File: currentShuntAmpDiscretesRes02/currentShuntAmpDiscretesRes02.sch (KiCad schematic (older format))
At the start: 17 parts, among them Q1 2N3906, Q2 2N3906, Q3 2N3906

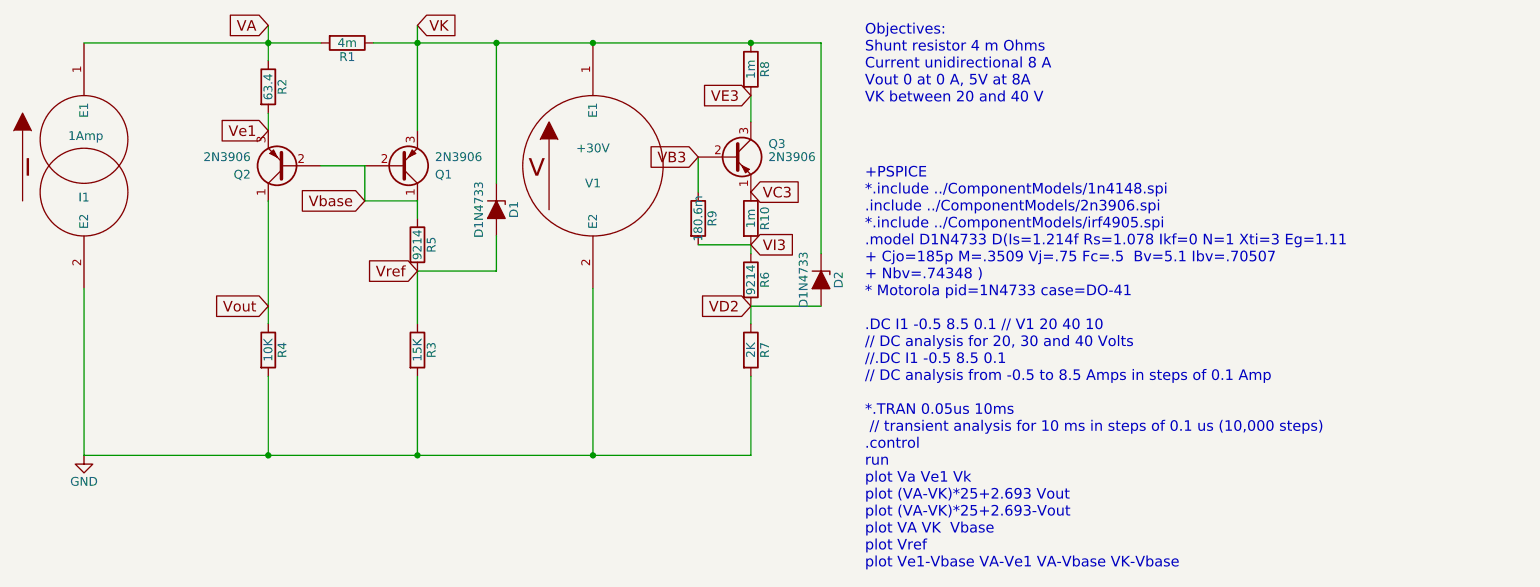
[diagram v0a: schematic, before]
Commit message: spice and spreadsheet models lined up approximately
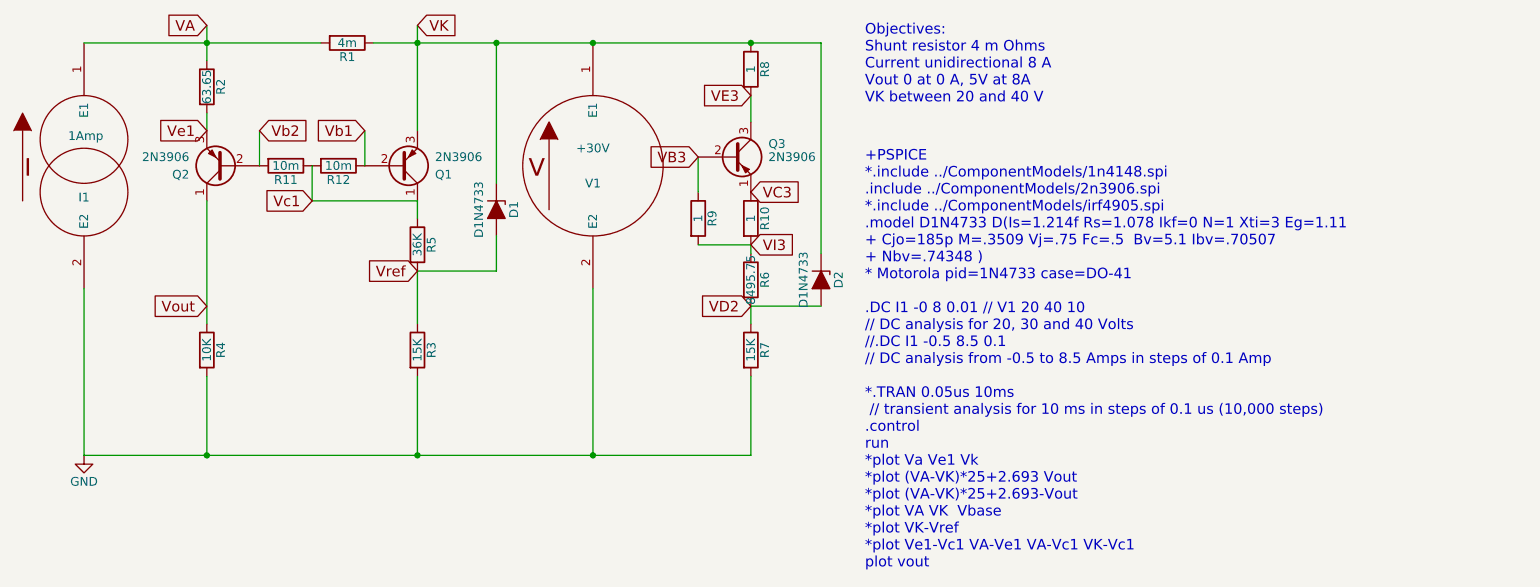
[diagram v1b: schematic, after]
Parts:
- added R11, R12: 10m, symbol R
- R10, R8: value 1m -> 1
- R2: value 63.4 -> 63.65
- R5: value 9214 -> 36K
- R6: value 9214 -> 8495.75
- R7: value 2K -> 15K
- R9: value 180.6m -> 1
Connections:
- net Vbase renamed Vc1
- net Vc1: now also R11.1, R12.2; no longer Q1.2 (B), Q2.2 (B)
- new net Vb1: Q1.2 (B), R12.1
- new net Vb2: Q2.2 (B), R11.2
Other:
- note added: "+PSPICE \n*.include ../ComponentModels/1n4148.spi\n.include ../ComponentModels/2n3906.spi\n*.include ../ComponentModels/irf4905.spi\n.model D1N4733 D(Is=1.214f Rs=1.078 Ikf=0 N=1 Xti=3 Eg=1.11\n+ Cjo=185p M=.3509 Vj=.75 Fc=.5 Bv=5.1 Ibv=.70507\n+ Nbv=.74348 )\n* Motorola pid=1N4733 case=DO-41\n\n.DC I1 -0 8 0.01 // V1 20 40 10 \n// DC analysis for 20, 30 and 40 Volts\n//.DC I1 -0.5 8.5 0.1\n// DC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"
- note removed: "+PSPICE \n*.include ../ComponentModels/1n4148.spi\n.include ../ComponentModels/2n3906.spi\n*.include ../ComponentModels/irf4905.spi\n.model D1N4733 D(Is=1.214f Rs=1.078 Ikf=0 N=1 Xti=3 Eg=1.11\n+ Cjo=185p M=.3509 Vj=.75 Fc=.5 Bv=5.1 Ibv=.70507\n+ Nbv=.74348 )\n* Motorola pid=1N4733 case=DO-41\n\n.DC I1 -0.5 8.5 0.1 // V1 20 40 10 \n// DC analysis for 20, 30 and 40 Volts\n//.DC I1 -0.5 8.5 0.1\n//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"
- moved on the sheet: R2, R4
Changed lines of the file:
@@
-$EndComp
-$Comp
-L Q_PNP_CBE Q2
-U 1 1 5AF15DB1
-P 2050 1400
-F 0 "Q2" H 2250 1450 50  0000 L CNN
-F 1 "2N3906" H 2250 1350 50  0000 L CNN
-F 2 "" H 2250 1500 50  0001 C CNN
-F 3 "" H 2050 1400 50  0001 C CNN
-	1    2050 1400
-	-1   0    0    1
 $EndComp
 $Comp
 L R R4
 U 1 1 5AF15DB2
-P 1950 2450
-F 0 "R4" V 2030 2450 50  0000 C CNN
-F 1 "10K" V 1950 2450 50  0000 C CNN
-F 2 "" V 1880 2450 50  0001 C CNN
-F 3 "" H 1950 2450 50  0001 C CNN
-	1    1950 2450
-	1    0    0    -1
-$EndComp
-Wire Wire Line
-	2500 1400 2500 1600
+P 1600 2450
+F 0 "R4" V 1680 2450 50  0000 C CNN
+F 1 "10K" V 1600 2450 50  0000 C CNN
+F 2 "" V 1530 2450 50  0001 C CNN
+F 3 "" H 1600 2450 50  0001 C CNN
+	1    1600 2450
+	1    0    0    -1
+$EndComp
+Wire Wire Line
+	2200 1400 2200 1600
 $Comp
 L Q_PNP_CBE Q1
@@
 P 2800 1850
 F 0 "R5" V 2880 1850 50  0000 C CNN
-F 1 "9214" V 2800 1850 50  0000 C CNN
+F 1 "36K" V 2800 1850 50  0000 C CNN
 F 2 "" V 2730 1850 50  0001 C CNN
 F 3 "" H 2800 1850 50  0001 C CNN
@@
 	900  3050 4700 3050
 Wire Wire Line
-	2500 1400 2250 1400
-Wire Wire Line
-	2500 1600 2800 1600
+	2200 1600 2800 1600
 Text Notes 5350 3700 0    60   ~ 0
-+PSPICE \n*.include ../ComponentModels/1n4148.spi\n.include ../ComponentModels/2n3906.spi\n*.include ../ComponentModels/irf4905.spi\n.model D1N4733 D(Is=1.214f Rs=1.078 Ikf=0 N=1 Xti=3 Eg=1.11\n+ Cjo=185p M=.3509 Vj=.75 Fc=.5  Bv=5.1 Ibv=.70507\n+ Nbv=.74348 )\n* Motorola pid=1N4733 case=DO-41\n\n.DC I1 -0.5 8.5 0.1 // V1 20 40 10 \n// DC analysis for 20, 30 and 40 Volts\n//.DC I1 -0.5 8.5 0.1\n// DC analysis from -0.5 to 8.5 Amps in steps of 0.1 Amp\n\n*.TRAN 0.05us 10ms\n // transient analysis for 10 ms in steps of 0.1 us (10,000 steps)\n.control\nrun\nplot Va Ve1 Vk\nplot (VA-VK)*25+2.693 Vout\nplot (VA-VK)*25+2.693-Vout\nplot VA VK  Vbase\nplot Vref\nplot Ve1-Vbase VA-Ve1 VA-Vbase VK-Vbase\n
++PSPICE \n*.include ../ComponentModels/1n4148.spi\n.include ../ComponentModels/2n3906.spi\n*.include ../ComponentModels/irf4905.spi\n.model D1N4733 D(Is=1.214f Rs=1.078 Ikf=0 N=1 Xti=3 Eg=1.11\n+ Cjo=185p M=.3509 Vj=.75 Fc=.5  Bv=5.1 Ibv=.70507\n+ Nbv=.74348 )\n* Motorola pid=1N4733 case=DO-41\n\n.DC I1 -0 8 0.01 // V1 20 40 10 \n// DC analysis for 20, 30 and 40 Volts\n//.DC I1 -0.5 8.5 0.1\n// DC analysis from -0.5 to 8.5 Amps in steps of 0.1 Amp\n\n*.TRAN 0.05us 10ms\n // transient analysis for 10 ms in steps of 0.1 us (10,000 steps)\n.control\nrun\n*plot Va Ve1 Vk\n*plot (VA-VK)*25+2.693 Vout\n*plot (VA-VK)*25+2.693-Vout\n*plot VA VK  Vbase\n*plot VK-Vref\n*plot Ve1-Vc1 VA-Ve1 VA-Vc1 VK-Vc1\nplot vout\n
 Wire Wire Line
 	2550 700  5100 700
@@
 	1    0    0    -1
 $EndComp
-Connection ~ 1950 3050
-Text GLabel 1950 600  0    60   Input ~ 0
+Text GLabel 1600 600  0    60   Input ~ 0
 VA
 Text GLabel 2800 600  2    60   Input ~ 0
 VK
-Connection ~ 1950 700
-Text GLabel 2500 1600 0    60   Input ~ 0
-Vbase
+Connection ~ 1600 700
+Text GLabel 2200 1600 0    60   Input ~ 0
+Vc1
 Wire Wire Line
 	900  2100 900  3050
 Wire Wire Line
 	3800 3050 3800 2100
-Text GLabel 1950 2200 0    60   Input ~ 0
+Text GLabel 1600 2200 0    60   Input ~ 0
 Vout
 $Comp
@@
 L R R2
 U 1 1 5AF15DB9
-P 1950 950
-F 0 "R2" V 2030 950 50  0000 C CNN
-F 1 "63.4" V 1950 950 50  0000 C CNN
-F 2 "" H 1950 950 50  0001 C CNN
-F 3 "" H 1950 950 50  0001 C CNN
-	1    1950 950
-	1    0    0    -1
-$EndComp
-Wire Wire Line
-	1950 2600 1950 3050
+P 1600 950
+F 0 "R2" V 1680 950 50  0000 C CNN
+F 1 "63.65" V 1600 950 50  0000 C CNN
+F 2 "" H 1600 950 50  0001 C CNN
+F 3 "" H 1600 950 50  0001 C CNN
+	1    1600 950
+	1    0    0    -1
+$EndComp
+Wire Wire Line
+	1600 2600 1600 3050
 Connection ~ 2800 3050
 Wire Wire Line
-	1950 600  1950 800
+	1600 600  1600 800
 Wire Wire Line
 	2800 600  2800 1200
 Wire Wire Line
-	1950 1100 1950 1200
+	1600 1100 1600 1200
 Wire Wire Line
 	2800 1600 2800 1700
 Wire Wire Line
-	1950 2300 1950 1600
+	1600 2300 1600 1600
 Text Notes 5350 1050 0    60   ~ 0
 Objectives:\nShunt resistor 4 m Ohms\nCurrent unidirectional 8 A\nVout 0 at 0 A, 5V at 8A\nVK between 20 and 40 V
-Text GLabel 1950 1200 0    60   Input ~ 0
+Text GLabel 1600 1200 0    60   Input ~ 0
 Ve1
 $Comp
@@
 P 4700 2050
 F 0 "R6" V 4780 2050 50  0000 C CNN
-F 1 "9214" V 4700 2050 50  0000 C CNN
+F 1 "8495.75" V 4700 2050 50  0000 C CNN
 F 2 "" V 4630 2050 50  0001 C CNN
 F 3 "" H 4700 2050 50  0001 C CNN
@@
 P 4700 2450
 F 0 "R7" V 4780 2450 50  0000 C CNN
-F 1 "2K" V 4700 2450 50  0000 C CNN
+F 1 "15K" V 4700 2450 50  0000 C CNN
 F 2 "" V 4630 2450 50  0001 C CNN
 F 3 "" H 4700 2450 50  0001 C CNN
@@
 P 4700 850
 F 0 "R8" V 4780 850 50  0000 C CNN
-F 1 "1m" V 4700 850 50  0000 C CNN
+F 1 "1" V 4700 850 50  0000 C CNN
 F 2 "" V 4630 850 50  0001 C CNN
 F 3 "" H 4700 850 50  0001 C CNN
@@
 P 4400 1700
 F 0 "R9" V 4480 1700 50  0000 C CNN
-F 1 "180.6m" V 4400 1700 50  0000 C CNN
+F 1 "1" V 4400 1700 50  0000 C CNN
 F 2 "" V 4330 1700 50  0001 C CNN
 F 3 "" H 4400 1700 50  0001 C CNN
@@
 P 4700 1700
 F 0 "R10" V 4780 1700 50  0000 C CNN
-F 1 "1m" V 4700 1700 50  0000 C CNN
+F 1 "1" V 4700 1700 50  0000 C CNN
 F 2 "" V 4630 1700 50  0001 C CNN
 F 3 "" H 4700 1700 50  0001 C CNN
@@
 Text GLabel 4700 1850 2    60   Input ~ 0
 VI3
+$Comp
+L R R11
+U 1 1 5AF22BCB
+P 2050 1400
+F 0 "R11" V 2130 1400 50  0000 C CNN
+F 1 "10m" V 2050 1400 50  0000 C CNN
+F 2 "" V 1980 1400 50  0001 C CNN
+F 3 "" H 2050 1400 50  0001 C CNN
+	1    2050 1400
+	0    1    1    0
+$EndComp
+Text GLabel 1900 1200 2    60   Input ~ 0
+Vb2
+Wire Wire Line
+	1900 1200 1900 1400
+$Comp
+L R R12
+U 1 1 5AF23799
+P 2350 1400
+F 0 "R12" V 2430 1400 50  0000 C CNN
+F 1 "10m" V 2350 1400 50  0000 C CNN
+F 2 "" V 2280 1400 50  0001 C CNN
+F 3 "" H 2350 1400 50  0001 C CNN
+	1    2350 1400
+	0    1    1    0
+$EndComp
+Text GLabel 2500 1200 0    60   Input ~ 0
+Vb1
+Wire Wire Line
+	2500 1200 2500 1400
+$Comp
+L Q_PNP_CBE Q2
+U 1 1 5AF24872
+P 1700 1400
+F 0 "Q2" H 1900 1450 50  0000 L CNN
+F 1 "2N3906" H 1900 1350 50  0000 L CNN
+F 2 "" H 1900 1500 50  0001 C CNN
+F 3 "" H 1700 1400 50  0001 C CNN
+	1    1700 1400
+	-1   0    0    1
+$EndComp
+Connection ~ 1600 3050
 $EndSCHEMATC
